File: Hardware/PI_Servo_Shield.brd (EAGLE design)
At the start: 65 x 30 mm, 89 parts, among them J1 RASPBERRYPI-40-PIN-GPIO_PTH_N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, J20 USB C, U2 PCA9306, U3 PCA9685, U5 CH340C

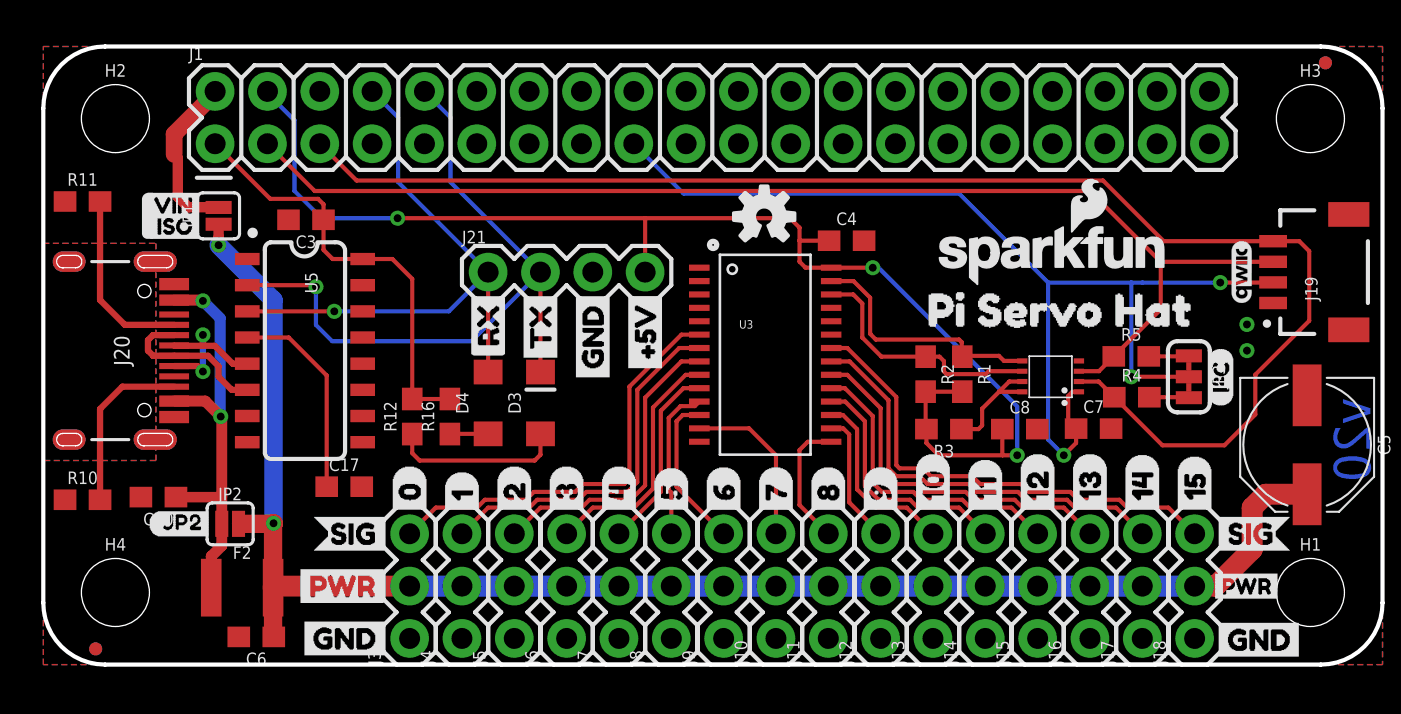
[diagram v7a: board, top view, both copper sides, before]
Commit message: locking fp on serial header, sch cleanup
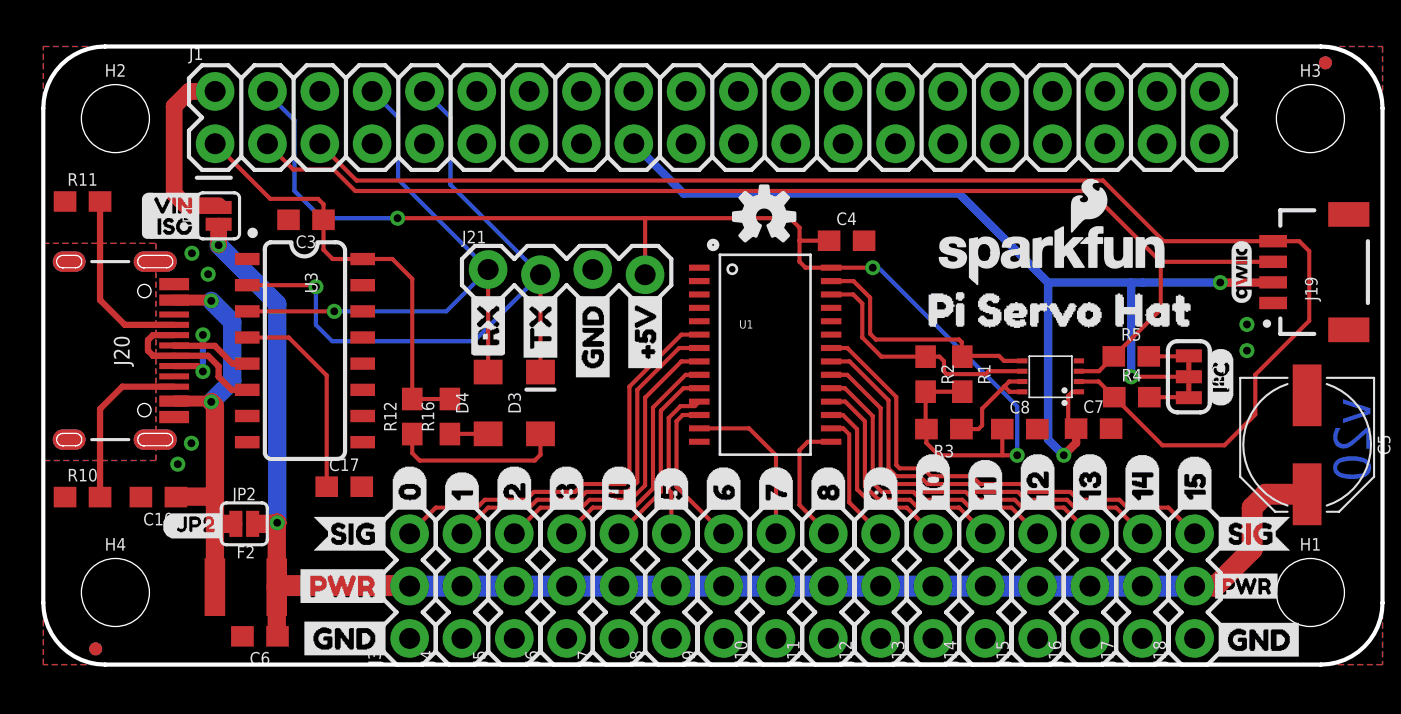
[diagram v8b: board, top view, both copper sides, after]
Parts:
- removed U5: CH340C, SparkFun-IC-Comms:SO016
- added U1: PCA9685, SparkFun-IC-Special-Function:TSSOP-28_4MM
- J1: value RASPBERRYPI-40-PIN-GPIO_PTH_NO_SHROUD -> RASPBERRYPI-40-PIN-GPIO
- J19: value (none) -> QWIIC
- J21: value (none) -> Serial; device SparkFun-Connectors:1X04 -> SparkFun-Connectors:1X04_LOCK
- U3: value PCA9685 -> CH340C; device SparkFun-IC-Special-Function:TSSOP-28_4MM -> SparkFun-IC-Comms:SO016
- moved U3 22.3 mm to (12.7, 15.2), turned to 270 degrees
- moved JP2 0.69 mm to (9.75, 6.83)
- moved U$33 0.67 mm to (5.77, 6.73)
- moved F2 0.18 mm to (9.83, 3.76)
- moved C6 0.18 mm to (10.5, 1.37)
- moved R10 0.13 mm to (1.91, 8.13)
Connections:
- net 3.3VA: now also U3.16; no longer U5.16
- net 5VB: now also U1.28; no longer U3.28
- net CH0: now also U1.6; no longer U3.6
- net CH1: now also U1.7; no longer U3.7
- net CH10: now also U1.17; no longer U3.17
- net CH11: now also U1.18; no longer U3.18
- net CH12: now also U1.19; no longer U3.19
- net CH13: now also U1.20; no longer U3.20
- net CH14: now also U1.21; no longer U3.21
- net CH15: now also U1.22; no longer U3.22
- net CH2: now also U1.8; no longer U3.8
- net CH3: now also U1.9; no longer U3.9
- net CH4: now also U1.10; no longer U3.10
- net CH5: now also U1.11; no longer U3.11
- net CH6: now also U1.12; no longer U3.12
- net CH7: now also U1.13; no longer U3.13
- net CH8: now also U1.15; no longer U3.15
- net CH9: now also U1.16; no longer U3.16
- net D+: now also U3.5; no longer U5.5
- net D-: now also U3.6; no longer U5.6
- net GND: now also U1.14, U1.23, U1.25, U3.1; no longer U3.14, U3.23, U3.25, U5.1
- net N$14: now also U3.4; no longer U5.4
- net N$3: now also U1.26; no longer U3.26
- net N$4: now also U1.27; no longer U3.27
- net RXI: now also U3.3; no longer U5.3
- net TXO: now also U3.2; no longer U5.2
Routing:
- net VIN: track 76.5 -> 75.6 mm
- net 5VA: track 8.21 -> 9.04 mm
- net VBUS: track 20.7 -> 21.4 mm
